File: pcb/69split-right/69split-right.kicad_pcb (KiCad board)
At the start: 2 copper layers, 343.5 x 105.4 mm, 142 parts, among them SW1 SW_Push, SW10 SW_Push, SW11 SW_Push, SW12 SW_Push, SW13 SW_Push, SW14 SW_Push, SW15 SW_Push, SW16 SW_Push, SW17 SW_Push, SW18 SW_Push, SW19 SW_Push, SW2 SW_Push, SW20 SW_Push, SW21 SW_Push, SW22 SW_Push, SW23 SW_Push, SW24 SW_Push, SW25 SW_Push, SW26 SW_Push, SW27 SW_Push, SW28 SW_Push, SW29 SW_Push, SW3 SW_Push, SW30 SW_Push, SW31 SW_Push, SW32 SW_Push, SW33 SW_Push, SW34 SW_Push, SW35 SW_Push, SW36 SW_Push, SW37 SW_Push, SW38 SW_Push, SW39 SW_Push, SW4 SW_Push, SW40 SW_Push, SW41 SW_Push, SW42 SW_Push, SW43 SW_Push, SW44 SW_Push, SW45 SW_Push, SW46 SW_Push, SW47 SW_Push, SW48 SW_Push, SW49 SW_Push, SW5 SW_Push, SW50 SW_Push, SW51 SW_Push, SW52 SW_Push, SW53 SW_Push, SW54 SW_Push, SW55 SW_Push, SW56 SW_Push, SW57 SW_Push, SW58 SW_Push, SW59 SW_Push, SW6 SW_Push, SW60 SW_Push, SW61 SW_Push, SW62 SW_Push, SW63 SW_Push, SW64 SW_Push, SW65 SW_Push, SW66 SW_Push, SW67 SW_Push, SW68 SW_Push, SW69 SW_Push, SW7 SW_Push, SW8 SW_Push, SW9 SW_Push

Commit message: Started changing things gain to use an I/O expander with I2C.
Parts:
- removed D40, D41, D42, D43, D44, D45, D46, D47, D48, D49, D50, D51, D52, D53, D54, D55, D56, D57, D58, D59, D60, D61, D62, D63, D64, D65, D66, D67, D68, D69: D, D_SOD-123
- removed ST14, ST43, ST45, ST63: MountingHole, Stabilizer_Cherry_MX_2.00u
- removed SW40, SW41, SW42, SW44, SW46, SW47, SW48, SW49, SW50, SW51, SW52, SW53, SW54, SW55, SW57, SW58, SW62, SW64, SW65, SW66, SW67, SW68, SW69: SW_Push, SW_Cherry_MX_PCB_1.00u
- removed SW43, SW45: SW_Push, SW_Cherry_MX_PCB_2.25u
- removed SW56: SW_Push, SW_Cherry_MX_PCB_1.75u
- removed SW59, SW60, SW61: SW_Push, SW_Cherry_MX_PCB_1.25u
- removed SW63: SW_Push, SW_Cherry_MX_PCB_2.75u
- added J1: Conn_01x03_Socket, Connector_PinSocket_2.54mm:PinSocket_1x03_P2.54mm_Horizontal, F.Cu at (230.7, 59.1)
- added J2: USB_C_Receptacle_24P, Connector_USB:USB_C_Receptacle_Amphenol_12401548E4-2A, B.Cu at (83.5, 40.0)
- added R1: 330R, Resistor_SMD:R_0603_1608Metric_Pad0.98x0.95mm_HandSolder, F.Cu at (225.6, 64.5)
- added R2: 330R, Resistor_SMD:R_0603_1608Metric_Pad0.98x0.95mm_HandSolder, F.Cu at (228.2, 64.5)
- D1, D10, D11, D12, D13, D14, D15, D16, D17, D18, D19, D2, D20, D21, D22, D23, D24, D25, D26, D27, D28, D29, D3, D30, D31, D32, D33, D34, D35, D36, D37, D38, D39, D4, D5, D6, D7, D8, D9: footprint D_SOD-123 -> Diode_THT:D_DO-35_SOD27_P7.62mm_Horizontal
- SW1: value SW_Push -> &,7,,F7; footprint SW_Cherry_MX_PCB_1.00u -> Button_Switch_Keyboard:SW_Cherry_MX_1.00u_PCB
- SW10: value SW_Push -> I; footprint SW_Cherry_MX_PCB_1.00u -> Button_Switch_Keyboard:SW_Cherry_MX_1.00u_PCB
- SW11: value SW_Push -> O; footprint SW_Cherry_MX_PCB_1.00u -> Button_Switch_Keyboard:SW_Cherry_MX_1.00u_PCB
- SW12: value SW_Push -> P; footprint SW_Cherry_MX_PCB_1.00u -> Button_Switch_Keyboard:SW_Cherry_MX_1.00u_PCB
- SW13: value SW_Push -> {,[; footprint SW_Cherry_MX_PCB_1.00u -> Button_Switch_Keyboard:SW_Cherry_MX_1.00u_PCB
- SW14: value SW_Push -> },]; footprint SW_Cherry_MX_PCB_2.00u -> Button_Switch_Keyboard:SW_Cherry_MX_1.00u_PCB
- SW15: value SW_Push -> Enter; footprint SW_Cherry_MX_PCB_1.00u -> Button_Switch_Keyboard:SW_Cherry_MX_ISOEnter_PCB
- SW16: value SW_Push -> Delete,Insert; footprint SW_Cherry_MX_PCB_1.50u -> Button_Switch_Keyboard:SW_Cherry_MX_1.00u_PCB
- SW17: value SW_Push -> H; footprint SW_Cherry_MX_PCB_1.00u -> Button_Switch_Keyboard:SW_Cherry_MX_1.00u_PCB
- SW18: value SW_Push -> J; footprint SW_Cherry_MX_PCB_1.00u -> Button_Switch_Keyboard:SW_Cherry_MX_1.00u_PCB
- SW19: value SW_Push -> K; footprint SW_Cherry_MX_PCB_1.00u -> Button_Switch_Keyboard:SW_Cherry_MX_1.00u_PCB
- SW2: value SW_Push -> *,8,,F8; footprint SW_Cherry_MX_PCB_1.00u -> Button_Switch_Keyboard:SW_Cherry_MX_1.00u_PCB
- SW20: value SW_Push -> L; footprint SW_Cherry_MX_PCB_1.00u -> Button_Switch_Keyboard:SW_Cherry_MX_1.00u_PCB
- SW21: value SW_Push -> :,;; footprint SW_Cherry_MX_PCB_1.00u -> Button_Switch_Keyboard:SW_Cherry_MX_1.00u_PCB
- SW22: value SW_Push -> @,'; footprint SW_Cherry_MX_PCB_1.00u -> Button_Switch_Keyboard:SW_Cherry_MX_1.00u_PCB
- SW23: value SW_Push -> #,~; footprint SW_Cherry_MX_PCB_1.00u -> Button_Switch_Keyboard:SW_Cherry_MX_1.00u_PCB
- SW24: value SW_Push -> Home,PgUp; footprint SW_Cherry_MX_PCB_1.00u -> Button_Switch_Keyboard:SW_Cherry_MX_1.00u_PCB
- SW25: value SW_Push -> N; footprint SW_Cherry_MX_PCB_1.00u -> Button_Switch_Keyboard:SW_Cherry_MX_1.00u_PCB
- SW26: value SW_Push -> M; footprint SW_Cherry_MX_PCB_1.00u -> Button_Switch_Keyboard:SW_Cherry_MX_1.00u_PCB
- SW27: value SW_Push -> <,,; footprint SW_Cherry_MX_PCB_1.00u -> Button_Switch_Keyboard:SW_Cherry_MX_1.00u_PCB
- SW28: value SW_Push -> >,.; footprint SW_Cherry_MX_PCB_1.00u -> Button_Switch_Keyboard:SW_Cherry_MX_1.00u_PCB
- SW29: value SW_Push -> ?,/; footprint SW_Cherry_MX_PCB_1.50u -> Button_Switch_Keyboard:SW_Cherry_MX_1.00u_PCB
- SW3: value SW_Push -> (,9,,F9; footprint SW_Cherry_MX_PCB_1.00u -> Button_Switch_Keyboard:SW_Cherry_MX_1.00u_PCB
- SW30: value SW_Push -> Shift; footprint SW_Cherry_MX_PCB_1.00u -> Button_Switch_Keyboard:SW_Cherry_MX_1.75u_PCB
- SW31: value SW_Push -> ↑; footprint SW_Cherry_MX_PCB_1.75u -> Button_Switch_Keyboard:SW_Cherry_MX_1.00u_PCB
- SW32: value SW_Push -> End,PgDn; footprint SW_Cherry_MX_PCB_1.00u -> Button_Switch_Keyboard:SW_Cherry_MX_1.00u_PCB
- SW33: value SW_Push -> Space; footprint SW_Cherry_MX_PCB_1.00u -> Button_Switch_Keyboard:SW_Cherry_MX_2.75u_PCB
- SW34: value SW_Push -> Alt,`,¬; footprint SW_Cherry_MX_PCB_1.00u -> Button_Switch_Keyboard:SW_Cherry_MX_1.25u_PCB
- SW35: value SW_Push -> Fn; footprint SW_Cherry_MX_PCB_1.00u -> Button_Switch_Keyboard:SW_Cherry_MX_1.25u_PCB
- SW36: value SW_Push -> Ctrl; footprint SW_Cherry_MX_PCB_1.00u -> Button_Switch_Keyboard:SW_Cherry_MX_1.25u_PCB
- SW37: value SW_Push -> ←; footprint SW_Cherry_MX_PCB_1.00u -> Button_Switch_Keyboard:SW_Cherry_MX_1.00u_PCB
- SW38: value SW_Push -> ↓; footprint SW_Cherry_MX_PCB_1.00u -> Button_Switch_Keyboard:SW_Cherry_MX_1.00u_PCB
- SW39: value SW_Push -> →; footprint SW_Cherry_MX_PCB_1.00u -> Button_Switch_Keyboard:SW_Cherry_MX_1.00u_PCB
- SW4: value SW_Push -> ),0,,F10; footprint SW_Cherry_MX_PCB_1.00u -> Button_Switch_Keyboard:SW_Cherry_MX_1.00u_PCB
- SW5: value SW_Push -> _,-,,F11; footprint SW_Cherry_MX_PCB_1.00u -> Button_Switch_Keyboard:SW_Cherry_MX_1.00u_PCB
- SW6: value SW_Push -> +,=,,F12; footprint SW_Cherry_MX_PCB_1.00u -> Button_Switch_Keyboard:SW_Cherry_MX_1.00u_PCB
- SW7: value SW_Push -> Backspace; footprint SW_Cherry_MX_PCB_1.00u -> Button_Switch_Keyboard:SW_Cherry_MX_2.00u_PCB
- SW8: value SW_Push -> Y; footprint SW_Cherry_MX_PCB_1.00u -> Button_Switch_Keyboard:SW_Cherry_MX_1.00u_PCB
- SW9: value SW_Push -> U; footprint SW_Cherry_MX_PCB_1.00u -> Button_Switch_Keyboard:SW_Cherry_MX_1.00u_PCB
- moved D16 240.1 mm to (237.3, 82.7)
- moved SW16 235.8 mm to (228.4, 72.6)
- moved D31 219.9 mm to (216.5, 120.7)
- moved SW31 216.8 mm to (209.4, 110.7)
- moved D32 214.5 mm to (237.2, 120.7)
- moved SW32 209.7 mm to (228.4, 110.7)
- moved SW29 134.0 mm to (157.0, 110.7)
- moved D29 133.1 mm to (166.0, 120.7)
- moved D30 132.4 mm to (190.6, 120.7)
- moved SW30 131.8 mm to (183.2, 110.7)
- moved D25 131.0 mm to (87.4, 120.7)
- moved D28 130.8 mm to (144.8, 120.7)
- moved D26 130.4 mm to (107.1, 120.7)
- moved D27 130.2 mm to (126.4, 120.7)
- moved SW27 129.7 mm to (118.9, 110.7)
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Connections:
- D1 pad 1: ROW0 -> /Right Keyboard Connector/ROW0
- D10 pad 1: ROW0 -> /Right Keyboard Connector/ROW1
- D11 pad 1: ROW0 -> /Right Keyboard Connector/ROW1
- D12 pad 1: ROW0 -> /Right Keyboard Connector/ROW1
- D13 pad 1: ROW0 -> /Right Keyboard Connector/ROW1
- D14 pad 1: ROW0 -> /Right Keyboard Connector/ROW1
- D15 pad 1: ROW0 -> /Right Keyboard Connector/ROW1
- D16 pad 1: ROW1 -> /Right Keyboard Connector/ROW1
- D17 pad 1: ROW1 -> /Right Keyboard Connector/ROW2
- D18 pad 1: ROW1 -> /Right Keyboard Connector/ROW2
- D19 pad 1: ROW1 -> /Right Keyboard Connector/ROW2
- D2 pad 1: ROW0 -> /Right Keyboard Connector/ROW0
- D20 pad 1: ROW1 -> /Right Keyboard Connector/ROW2
- D21 pad 1: ROW1 -> /Right Keyboard Connector/ROW2
- D22 pad 1: ROW1 -> /Right Keyboard Connector/ROW2
- D23 pad 1: ROW1 -> /Right Keyboard Connector/ROW2
- D24 pad 1: ROW1 -> /Right Keyboard Connector/ROW2
- D25 pad 1: ROW1 -> /Right Keyboard Connector/ROW3
- D26 pad 1: ROW1 -> /Right Keyboard Connector/ROW3
- D27 pad 1: ROW1 -> /Right Keyboard Connector/ROW3
- D28 pad 1: ROW1 -> /Right Keyboard Connector/ROW3
- D29 pad 1: ROW1 -> /Right Keyboard Connector/ROW3
- D3 pad 1: ROW0 -> /Right Keyboard Connector/ROW0
- D30 pad 1: ROW1 -> /Right Keyboard Connector/ROW3
- D31 pad 1: ROW2 -> /Right Keyboard Connector/ROW3
- D32 pad 1: ROW2 -> /Right Keyboard Connector/ROW3
- D33 pad 1: ROW2 -> /Right Keyboard Connector/ROW4
- D34 pad 1: ROW2 -> /Right Keyboard Connector/ROW4
- D35 pad 1: ROW2 -> /Right Keyboard Connector/ROW4
- D36 pad 1: ROW2 -> /Right Keyboard Connector/ROW4
- D37 pad 1: ROW2 -> /Right Keyboard Connector/ROW4
- D38 pad 1: ROW2 -> /Right Keyboard Connector/ROW4
- D39 pad 1: ROW2 -> /Right Keyboard Connector/ROW4
- D4 pad 1: ROW0 -> /Right Keyboard Connector/ROW0
- D5 pad 1: ROW0 -> /Right Keyboard Connector/ROW0
- D6 pad 1: ROW0 -> /Right Keyboard Connector/ROW0
- D7 pad 1: ROW0 -> /Right Keyboard Connector/ROW0
- D8 pad 1: ROW0 -> /Right Keyboard Connector/ROW1
- D9 pad 1: ROW0 -> /Right Keyboard Connector/ROW1
- SW1 pad 1: COL0 -> /Right Keyboard Connector/COL6
- SW10 pad 1: COL11 -> /Right Keyboard Connector/COL8
- SW11 pad 1: COL12 -> /Right Keyboard Connector/COL9
- SW12 pad 1: COL13 -> /Right Keyboard Connector/COL10
- SW13 pad 1: COL14 -> /Right Keyboard Connector/COL11
- SW14 pad 1: COL15 -> /Right Keyboard Connector/COL12
- SW15 pad 1: COL17 -> /Right Keyboard Connector/COL13
- SW16 pad 1: COL0 -> /Right Keyboard Connector/COL14
- SW17 pad 1: COL2 -> /Right Keyboard Connector/COL6
- SW18 pad 1: COL3 -> /Right Keyboard Connector/COL7
- SW19 pad 1: COL4 -> /Right Keyboard Connector/COL8
- SW2 pad 1: COL1 -> /Right Keyboard Connector/COL7
- SW20 pad 1: COL5 -> /Right Keyboard Connector/COL9
- SW21 pad 1: COL6 -> /Right Keyboard Connector/COL10
- SW22 pad 1: COL8 -> /Right Keyboard Connector/COL11
- SW23 pad 1: COL9 -> /Right Keyboard Connector/COL12
- SW24 pad 1: COL10 -> /Right Keyboard Connector/COL14
- SW25 pad 1: COL11 -> /Right Keyboard Connector/COL7
- SW26 pad 1: COL12 -> /Right Keyboard Connector/COL8
- SW27 pad 1: COL13 -> /Right Keyboard Connector/COL9
- SW28 pad 1: COL14 -> /Right Keyboard Connector/COL10
- SW29 pad 1: COL15 -> /Right Keyboard Connector/COL11
- SW3 pad 1: COL2 -> /Right Keyboard Connector/COL8
- SW30 pad 1: COL17 -> /Right Keyboard Connector/COL12
- SW31 pad 1: COL0 -> /Right Keyboard Connector/COL13
- SW32 pad 1: COL2 -> /Right Keyboard Connector/COL14
- SW33 pad 1: COL3 -> /Right Keyboard Connector/COL7
- SW34 pad 1: COL4 -> /Right Keyboard Connector/COL9
- SW35 pad 1: COL5 -> /Right Keyboard Connector/COL10
- SW36 pad 1: COL6 -> /Right Keyboard Connector/COL11
- SW37 pad 1: COL8 -> /Right Keyboard Connector/COL12
- SW38 pad 1: COL9 -> /Right Keyboard Connector/COL13
- SW39 pad 1: COL10 -> /Right Keyboard Connector/COL14
- SW4 pad 1: COL3 -> /Right Keyboard Connector/COL9
- SW5 pad 1: COL4 -> /Right Keyboard Connector/COL10
- SW6 pad 1: COL5 -> /Right Keyboard Connector/COL11
- SW7 pad 1: COL6 -> /Right Keyboard Connector/COL13
- SW8 pad 1: COL9 -> /Right Keyboard Connector/COL6
- SW9 pad 1: COL10 -> /Right Keyboard Connector/COL7
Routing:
- added copper zone on B.Cu, net GND
- added copper zone on F.Cu, net GND
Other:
- board size 343.5 x 105.4 mm -> 186.1 x 105.3 mm

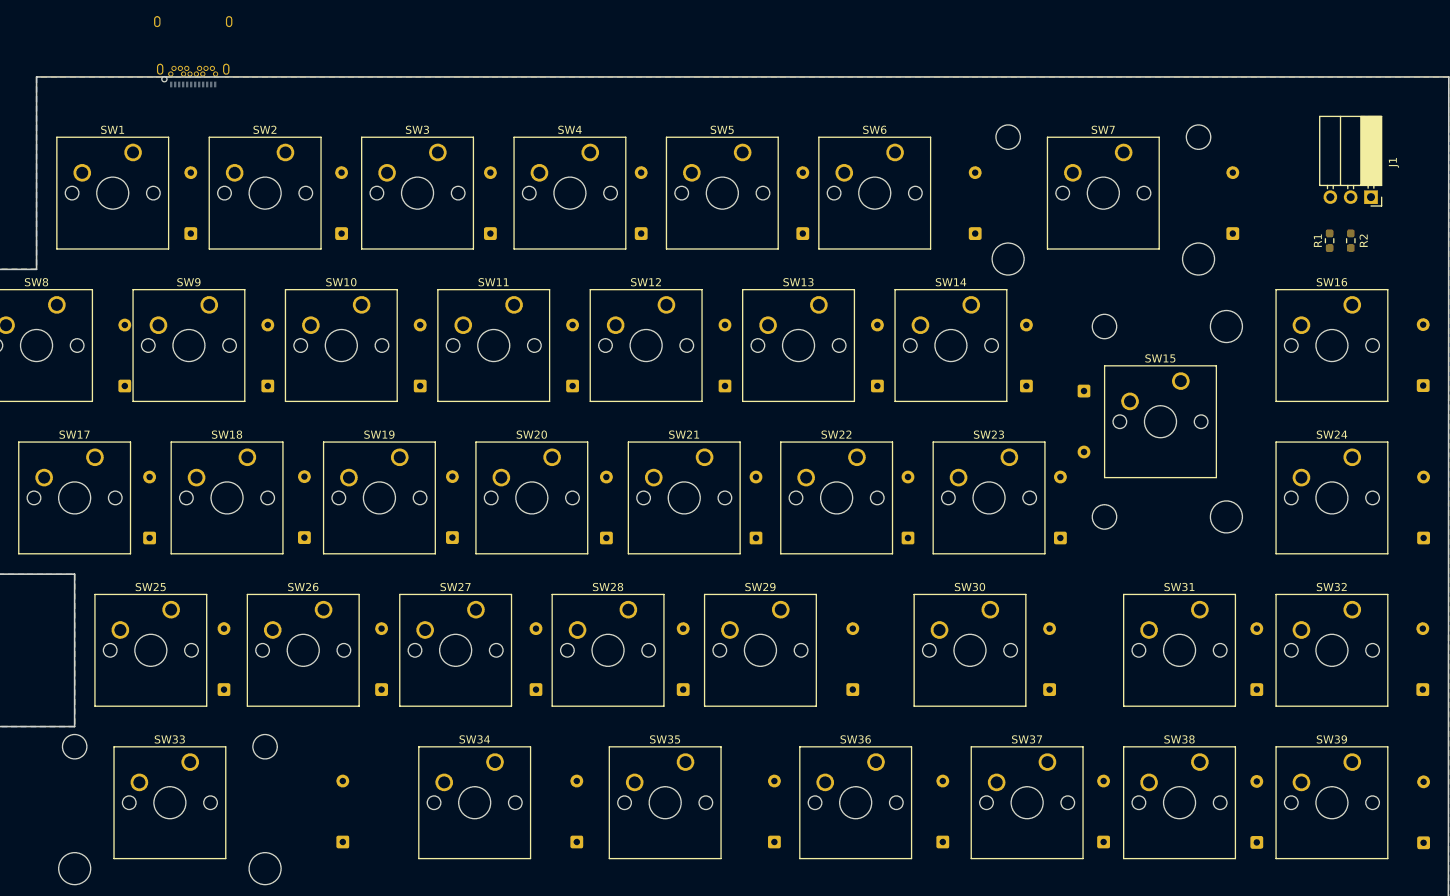
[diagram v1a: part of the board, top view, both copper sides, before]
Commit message: Continuing with I/O expander integration.
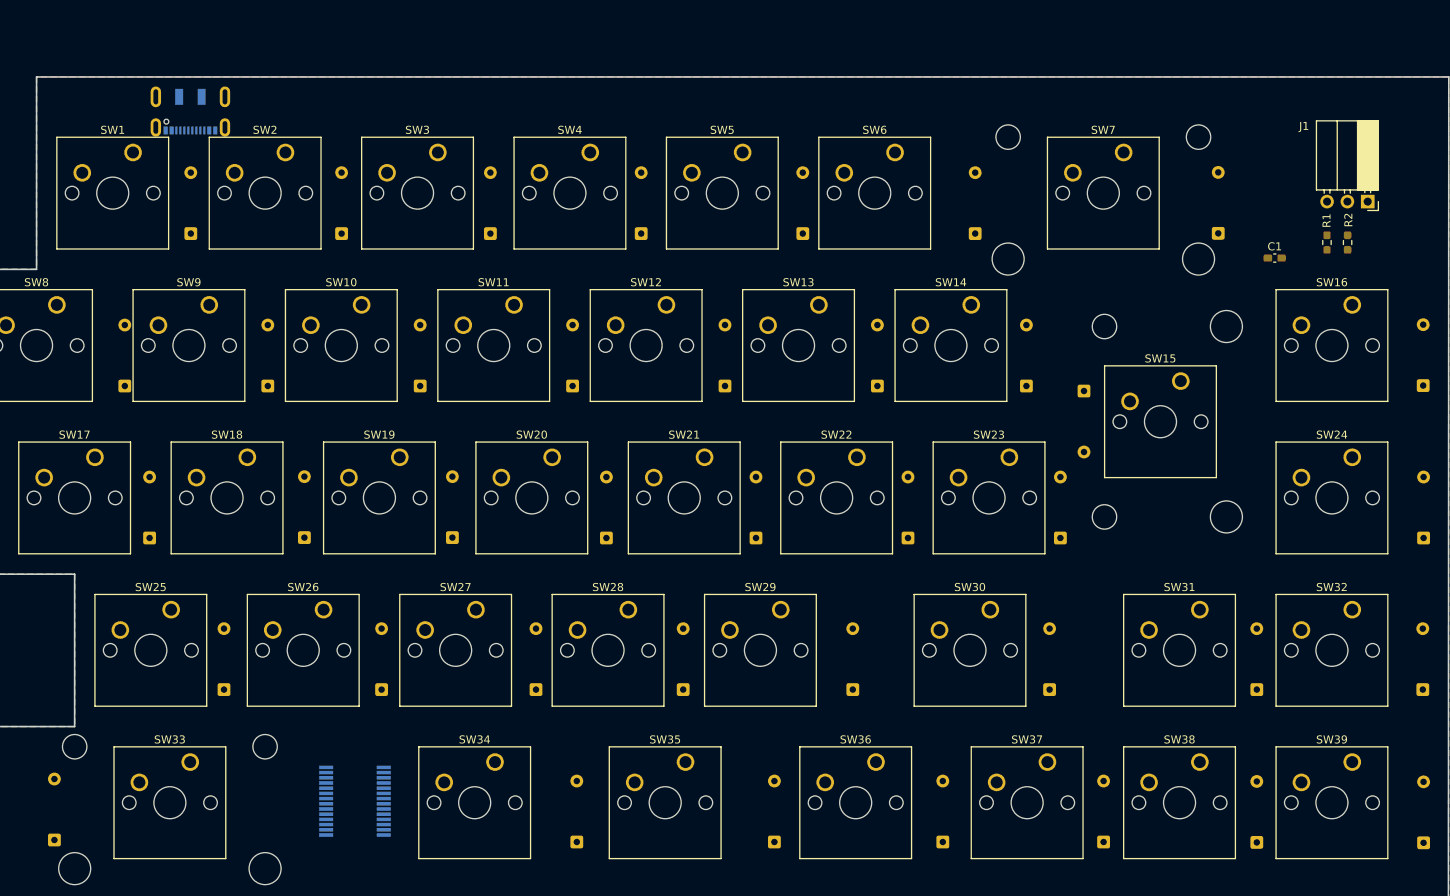
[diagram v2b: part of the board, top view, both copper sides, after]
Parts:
- added C1: 1u, Capacitor_SMD:C_0603_1608Metric_Pad1.08x0.95mm_HandSolder, F.Cu at (218.7, 66.7)
- added U1: MCP23017_SS, Package_SO:SSOP-28_5.3x10.2mm_P0.65mm, B.Cu at (103.7, 134.6)
- J2: value USB_C_Receptacle_24P -> USB_C_Receptacle_USB2.0_16P; footprint Connector_USB:USB_C_Receptacle_Amphenol_12401548E4-2A -> Connector_USB:USB_C_Receptacle_JAE_DX07S016JA1R1500
- moved D33 36.1 mm to (66.2, 139.4)
- moved J2 7.72 mm to (83.2, 47.7)
- moved D7 1.82 mm to (211.7, 63.6)
- moved J1 0.69 mm to (230.3, 59.6)
- moved R2 0.46 mm to (227.8, 64.8)
- moved R1 0.40 mm to (225.2, 64.8)
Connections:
- D1 pad 1: /Right Keyboard Connector/ROW0 -> /Right Matrix/ROW0
- D10 pad 1: /Right Keyboard Connector/ROW1 -> /Right Matrix/ROW1
- D11 pad 1: /Right Keyboard Connector/ROW1 -> /Right Matrix/ROW1
- D12 pad 1: /Right Keyboard Connector/ROW1 -> /Right Matrix/ROW1
- D13 pad 1: /Right Keyboard Connector/ROW1 -> /Right Matrix/ROW1
- D14 pad 1: /Right Keyboard Connector/ROW1 -> /Right Matrix/ROW1
- D15 pad 1: /Right Keyboard Connector/ROW1 -> /Right Matrix/ROW1
- D16 pad 1: /Right Keyboard Connector/ROW1 -> /Right Matrix/ROW1
- D17 pad 1: /Right Keyboard Connector/ROW2 -> /Right Matrix/ROW2
- D18 pad 1: /Right Keyboard Connector/ROW2 -> /Right Matrix/ROW2
- D19 pad 1: /Right Keyboard Connector/ROW2 -> /Right Matrix/ROW2
- D2 pad 1: /Right Keyboard Connector/ROW0 -> /Right Matrix/ROW0
- D20 pad 1: /Right Keyboard Connector/ROW2 -> /Right Matrix/ROW2
- D21 pad 1: /Right Keyboard Connector/ROW2 -> /Right Matrix/ROW2
- D22 pad 1: /Right Keyboard Connector/ROW2 -> /Right Matrix/ROW2
- D23 pad 1: /Right Keyboard Connector/ROW2 -> /Right Matrix/ROW2
- D24 pad 1: /Right Keyboard Connector/ROW2 -> /Right Matrix/ROW2
- D25 pad 1: /Right Keyboard Connector/ROW3 -> /Right Matrix/ROW3
- D26 pad 1: /Right Keyboard Connector/ROW3 -> /Right Matrix/ROW3
- D27 pad 1: /Right Keyboard Connector/ROW3 -> /Right Matrix/ROW3
- D28 pad 1: /Right Keyboard Connector/ROW3 -> /Right Matrix/ROW3
- D29 pad 1: /Right Keyboard Connector/ROW3 -> /Right Matrix/ROW3
- D3 pad 1: /Right Keyboard Connector/ROW0 -> /Right Matrix/ROW0
- D30 pad 1: /Right Keyboard Connector/ROW3 -> /Right Matrix/ROW3
- D31 pad 1: /Right Keyboard Connector/ROW3 -> /Right Matrix/ROW3
- D32 pad 1: /Right Keyboard Connector/ROW3 -> /Right Matrix/ROW3
- D33 pad 1: /Right Keyboard Connector/ROW4 -> /Right Matrix/ROW4
- D34 pad 1: /Right Keyboard Connector/ROW4 -> /Right Matrix/ROW4
- D35 pad 1: /Right Keyboard Connector/ROW4 -> /Right Matrix/ROW4
- D36 pad 1: /Right Keyboard Connector/ROW4 -> /Right Matrix/ROW4
- D37 pad 1: /Right Keyboard Connector/ROW4 -> /Right Matrix/ROW4
- D38 pad 1: /Right Keyboard Connector/ROW4 -> /Right Matrix/ROW4
- D39 pad 1: /Right Keyboard Connector/ROW4 -> /Right Matrix/ROW4
- D4 pad 1: /Right Keyboard Connector/ROW0 -> /Right Matrix/ROW0
- D5 pad 1: /Right Keyboard Connector/ROW0 -> /Right Matrix/ROW0
- D6 pad 1: /Right Keyboard Connector/ROW0 -> /Right Matrix/ROW0
- D7 pad 1: /Right Keyboard Connector/ROW0 -> /Right Matrix/ROW0
- D8 pad 1: /Right Keyboard Connector/ROW1 -> /Right Matrix/ROW1
- D9 pad 1: /Right Keyboard Connector/ROW1 -> /Right Matrix/ROW1
- J2 pad A4: /GPIO Outputs/GPIO_OUT_PB7 -> VCC
- J2 pad A5: /Right Keyboard Connector/ROW0 -> /GPIO Outputs/GPIO_OUT_PB7
- J2 pad A6: /Right Keyboard Connector/ROW4 -> /IO Expander/SCL
- J2 pad A7: /Right Keyboard Connector/ROW2 -> /IO Expander/SDA
- J2 pad A8: /Right Keyboard Connector/COL13 -> /GPIO Outputs/GPIO_OUT_PB6
- J2 pad A9: /GPIO Outputs/GPIO_OUT_PB6 -> VCC
- J2 pad B4: /GPIO Outputs/GPIO_OUT_PB7 -> VCC
- J2 pad B5: /Right Keyboard Connector/ROW1 -> /GPIO Outputs/GPIO_OUT_PB7
- J2 pad B6: /Right Keyboard Connector/ROW4 -> /IO Expander/SCL
- J2 pad B7: /Right Keyboard Connector/ROW3 -> /IO Expander/SDA
- J2 pad B8: /Right Keyboard Connector/COL14 -> /GPIO Outputs/GPIO_OUT_PB6
- J2 pad B9: /GPIO Outputs/GPIO_OUT_PB6 -> VCC
- SW1 pad 1: /Right Keyboard Connector/COL6 -> /IO Expander/COL6
- SW10 pad 1: /Right Keyboard Connector/COL8 -> /IO Expander/COL8
- SW11 pad 1: /Right Keyboard Connector/COL9 -> /IO Expander/COL9
- SW12 pad 1: /Right Keyboard Connector/COL10 -> /IO Expander/COL10
- SW13 pad 1: /Right Keyboard Connector/COL11 -> /IO Expander/COL11
- SW14 pad 1: /Right Keyboard Connector/COL12 -> /IO Expander/COL12
- SW15 pad 1: /Right Keyboard Connector/COL13 -> /IO Expander/COL13
- SW16 pad 1: /Right Keyboard Connector/COL14 -> /IO Expander/COL14
- SW17 pad 1: /Right Keyboard Connector/COL6 -> /IO Expander/COL6
- SW18 pad 1: /Right Keyboard Connector/COL7 -> /IO Expander/COL7
- SW19 pad 1: /Right Keyboard Connector/COL8 -> /IO Expander/COL8
- SW2 pad 1: /Right Keyboard Connector/COL7 -> /IO Expander/COL7
- SW20 pad 1: /Right Keyboard Connector/COL9 -> /IO Expander/COL9
- SW21 pad 1: /Right Keyboard Connector/COL10 -> /IO Expander/COL10
- SW22 pad 1: /Right Keyboard Connector/COL11 -> /IO Expander/COL11
- SW23 pad 1: /Right Keyboard Connector/COL12 -> /IO Expander/COL12
- SW24 pad 1: /Right Keyboard Connector/COL14 -> /IO Expander/COL14
- SW25 pad 1: /Right Keyboard Connector/COL7 -> /IO Expander/COL7
- SW26 pad 1: /Right Keyboard Connector/COL8 -> /IO Expander/COL8
- SW27 pad 1: /Right Keyboard Connector/COL9 -> /IO Expander/COL9
- SW28 pad 1: /Right Keyboard Connector/COL10 -> /IO Expander/COL10
- SW29 pad 1: /Right Keyboard Connector/COL11 -> /IO Expander/COL11
- SW3 pad 1: /Right Keyboard Connector/COL8 -> /IO Expander/COL8
- SW30 pad 1: /Right Keyboard Connector/COL12 -> /IO Expander/COL12
- SW31 pad 1: /Right Keyboard Connector/COL13 -> /IO Expander/COL13
- SW32 pad 1: /Right Keyboard Connector/COL14 -> /IO Expander/COL14
- SW33 pad 1: /Right Keyboard Connector/COL7 -> /IO Expander/COL7
- SW34 pad 1: /Right Keyboard Connector/COL9 -> /IO Expander/COL9
- SW35 pad 1: /Right Keyboard Connector/COL10 -> /IO Expander/COL10
- SW36 pad 1: /Right Keyboard Connector/COL11 -> /IO Expander/COL11
- SW37 pad 1: /Right Keyboard Connector/COL12 -> /IO Expander/COL12
- SW38 pad 1: /Right Keyboard Connector/COL13 -> /IO Expander/COL13
- SW39 pad 1: /Right Keyboard Connector/COL14 -> /IO Expander/COL14
- SW4 pad 1: /Right Keyboard Connector/COL9 -> /IO Expander/COL9
- SW5 pad 1: /Right Keyboard Connector/COL10 -> /IO Expander/COL10
- SW6 pad 1: /Right Keyboard Connector/COL11 -> /IO Expander/COL11
- SW7 pad 1: /Right Keyboard Connector/COL13 -> /IO Expander/COL13
- SW8 pad 1: /Right Keyboard Connector/COL6 -> /IO Expander/COL6
- SW9 pad 1: /Right Keyboard Connector/COL7 -> /IO Expander/COL7
